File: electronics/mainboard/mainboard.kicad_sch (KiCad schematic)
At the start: 24 parts, among them Q1 TSM250N02CX_RFG, Q2 TSM250N02CX_RFG, SW1 SW_Push, SW10 SW_Push, SW11 SW_Push, SW12 SW_Push, SW13 SW_Push, SW14 SW_Push, SW15 SW_Push, SW2 SW_Push, SW3 SW_Push, SW4 SW_Push, SW5 SW_Push, SW6 SW_Push, SW7 SW_Push, SW8 SW_Push, SW9 SW_Push, U1 1022

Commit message: integrate workflow for automatic mainboard production data creation and releases
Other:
- title: (none) -> Mainboard
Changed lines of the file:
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@@
 (kicad_sch (version 20211123) (generator eeschema)
   (paper "A4")
+  (title_block
+    (title "Mainboard")
+    (comment 1 "${PROJECT}")
+    (comment 2 "${PROJECT-URL}")
+    (comment 3 "${GIT-COMMIT-HASH}")
+    (comment 4 "${GIT-COMMIT-TAG}")
+  )
   (junction (at 76.2 48.26) (diameter 0) (color 0 0 0 0)
   )

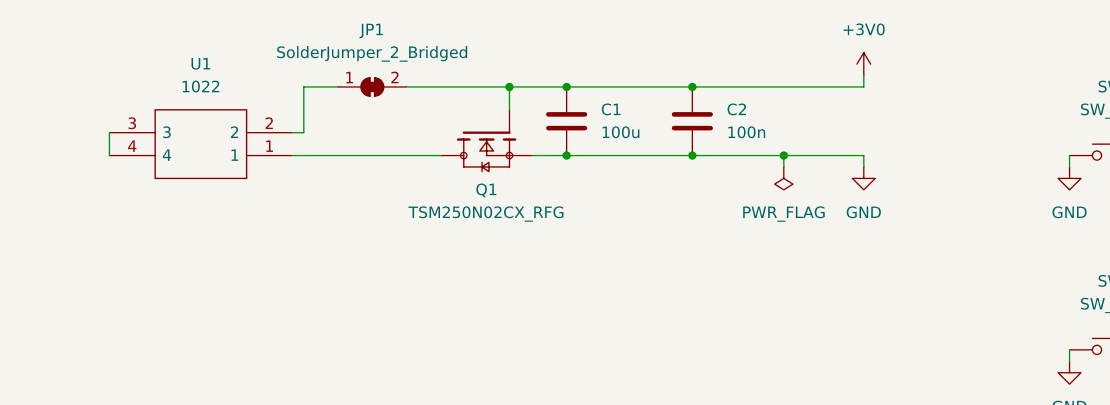
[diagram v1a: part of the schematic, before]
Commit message: add a fuse
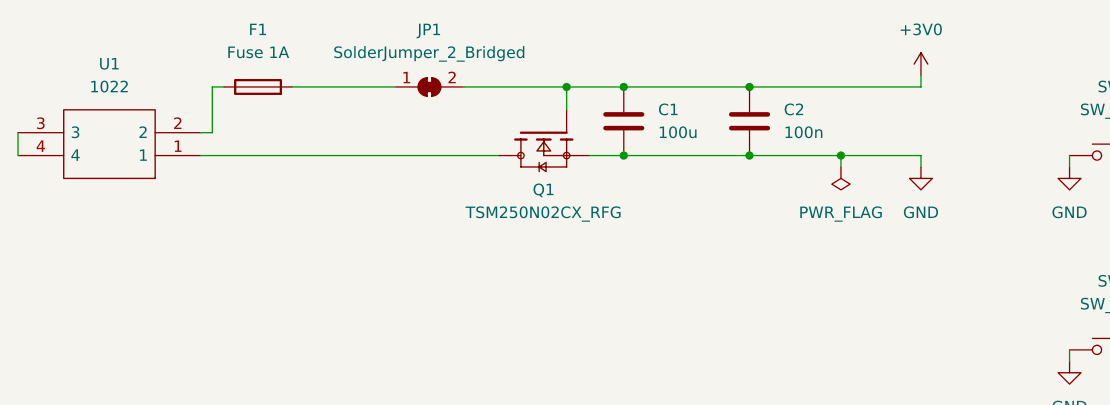
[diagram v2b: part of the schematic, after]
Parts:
- added F1: Fuse 1A, Fuse:Fuse_0805_2012Metric, symbol Device:Fuse
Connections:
- net at U1.2: now also F1.1; no longer JP1.1 (A)
- new net: F1.2, JP1.1 (A)
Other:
- moved on the sheet: C1, C2, JP1, Q1, U1

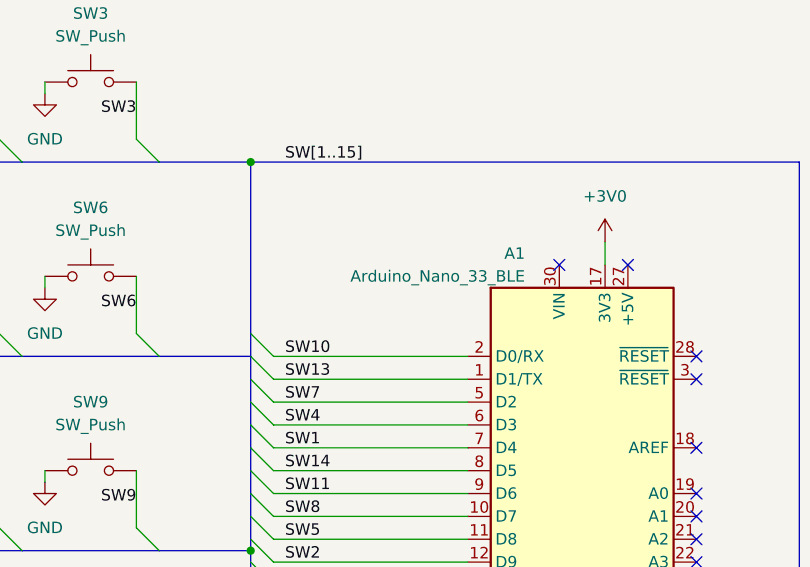
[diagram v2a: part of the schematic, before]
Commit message: add note to schematic about interchanged D0 and D1
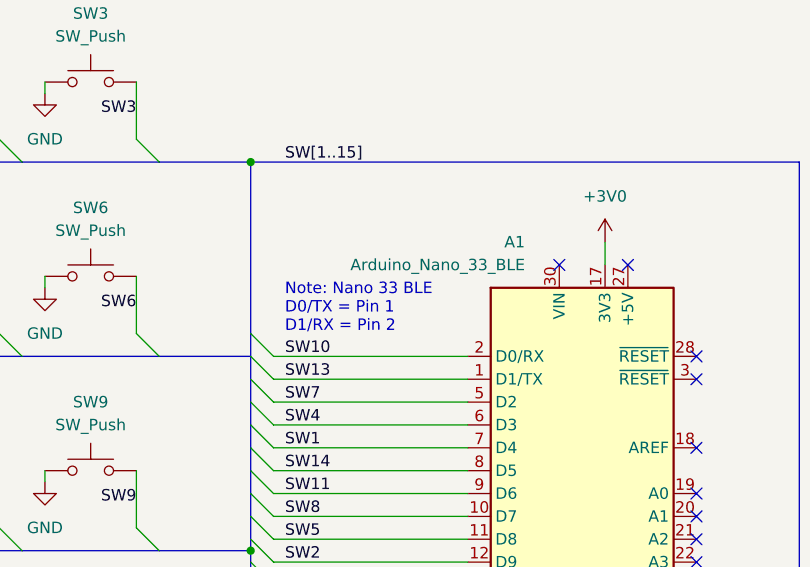
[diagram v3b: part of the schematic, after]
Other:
- note added: "Note: Nano 33 BLE D0/TX = Pin 1 D1/RX = Pin 2"
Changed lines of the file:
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@@
     (stroke (width 0) (type default) (color 0 0 0 0))
+  )
+  (text "Note: Nano 33 BLE\nD0/TX = Pin 1\nD1/RX = Pin 2" (at 189.23 76.2 0)
+    (effects (font (size 1.27 1.27)) (justify left bottom))
   )
   (label "SW5" (at 157.48 73.66 180)
@@
   (symbol (lib_id "MCU_Module:Arduino_Nano_v3.x") (at 222.25 93.98 0) (unit 1)
     (in_bom yes) (on_board yes)
-    (property "Reference" "A1" (id 0) (at 215.9 67.31 0)
+    (property "Reference" "A1" (id 0) (at 215.9 66.04 0)
       (effects (font (size 1.27 1.27)) (justify right))
     )
-    (property "Value" "Arduino_Nano_33_BLE" (id 1) (at 215.9 69.85 0)
+    (property "Value" "Arduino_Nano_33_BLE" (id 1) (at 215.9 68.58 0)
       (effects (font (size 1.27 1.27)) (justify right))
     )

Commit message: some changes
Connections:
- net at A1.26 (A7): no longer Q2.1

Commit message: update symbols
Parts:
- Q1, Q2: footprint TSM250N02CX_RFG:TRANS_TSM250N02CX_RFG -> TRANS_TSM250N02CX_RFG
- U1: footprint SamacSys:1022 -> 1022
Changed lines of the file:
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@@
       (effects (font (size 1.27 1.27)))
     )
-    (property "Footprint" "TSM250N02CX_RFG:TRANS_TSM250N02CX_RFG" (at 73.66 45.72 0)
+    (property "Footprint" "TRANS_TSM250N02CX_RFG" (at 73.66 45.72 0)
       (effects (font (size 1.27 1.27)) (justify left bottom) hide)
     )
@@
       (effects (font (size 1.27 1.27)))
     )
-    (property "Footprint" "SamacSys:1022" (at 19.05 50.8 0)
+    (property "Footprint" "1022" (at 19.05 50.8 0)
       (effects (font (size 1.27 1.27)) (justify left) hide)
     )
@@
     )
   )
-  (symbol (lib_id "TSM250N02CX_RFG:TSM250N02CX_RFG") (at 254 109.22 0) (unit 1)
+  (symbol (lib_name "TSM250N02CX_RFG_1") (lib_id "TSM250N02CX_RFG:TSM250N02CX_RFG") (at 254 109.22 0) (unit 1)
     (in_bom yes) (on_board yes) (dnp no) (fields_autoplaced)
     (property "Reference" "Q2" (at 259.08 107.9499 0)
@@
       (effects (font (size 1.27 1.27)) (justify left))
     )
-    (property "Footprint" "TSM250N02CX_RFG:TRANS_TSM250N02CX_RFG" (at 254 109.22 0)
+    (property "Footprint" "TRANS_TSM250N02CX_RFG" (at 254 109.22 0)
       (effects (font (size 1.27 1.27)) (justify left bottom) hide)
     )

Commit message: error corrections
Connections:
- net at A1.26 (A7): now also Q2.1
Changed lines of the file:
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@@
+    (stroke (width 0) (type default))
+  )
+  (wire (pts (xy 234.95 111.76) (xy 251.46 111.76))
     (stroke (width 0) (type default))
   )
